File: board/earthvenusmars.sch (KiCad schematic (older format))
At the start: 30 parts, among them J1 Conn_01x05_Female, J4 Conn_01x04, SW1 SW_SPST, SW2 SW_SPST, U1 ATSAMD21G18A-AU, U2 MIC5504-3.3YM5, Y1 32768Hz

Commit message: change 1uF cap to an 0603 because the 0805 one was so thick it was impacting the case design
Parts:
- C10, C13, C7, C9: footprint Capacitor_SMD:C_0805_2012Metric -> Capacitor_SMD:C_0603_1608Metric
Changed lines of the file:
@@
 F 0 "C7" H 5408 2096 50  0000 R CNN
 F 1 "1µF" H 5408 2005 50  0000 R CNN
-F 2 "Capacitor_SMD:C_0805_2012Metric" H 5500 2050 50  0001 C CNN
+F 2 "Capacitor_SMD:C_0603_1608Metric" H 5500 2050 50  0001 C CNN
 F 3 "~" H 5500 2050 50  0001 C CNN
 	1    5500 2050
@@
 F 0 "C9" H 1058 1446 50  0000 R CNN
 F 1 "1µF" H 1058 1355 50  0000 R CNN
-F 2 "Capacitor_SMD:C_0805_2012Metric" H 1150 1400 50  0001 C CNN
+F 2 "Capacitor_SMD:C_0603_1608Metric" H 1150 1400 50  0001 C CNN
 F 3 "~" H 1150 1400 50  0001 C CNN
 	1    1150 1400
@@
 F 0 "C10" H 2308 1446 50  0000 R CNN
 F 1 "1µF" H 2308 1355 50  0000 R CNN
-F 2 "Capacitor_SMD:C_0805_2012Metric" H 2400 1400 50  0001 C CNN
+F 2 "Capacitor_SMD:C_0603_1608Metric" H 2400 1400 50  0001 C CNN
 F 3 "~" H 2400 1400 50  0001 C CNN
 	1    2400 1400
@@
 F 0 "C13" H 1150 2950 50  0000 L CNN
 F 1 "1uF" H 1100 2750 50  0000 L CNN
-F 2 "Capacitor_SMD:C_0805_2012Metric" H 1188 2700 50  0001 C CNN
+F 2 "Capacitor_SMD:C_0603_1608Metric" H 1188 2700 50  0001 C CNN
 F 3 "~" H 1150 2850 50  0001 C CNN
 	1    1150 2850

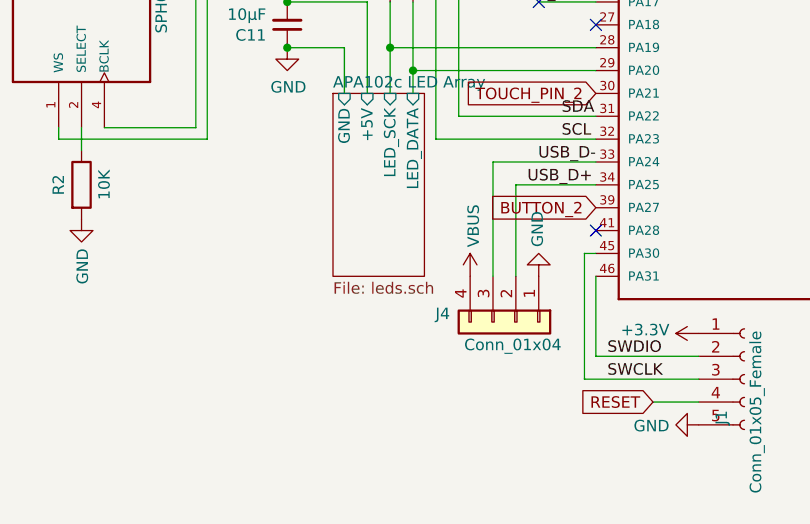
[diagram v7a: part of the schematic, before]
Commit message: add a usb-micro port (I know). including both usb styles on this prototype stage to try them both out and compare
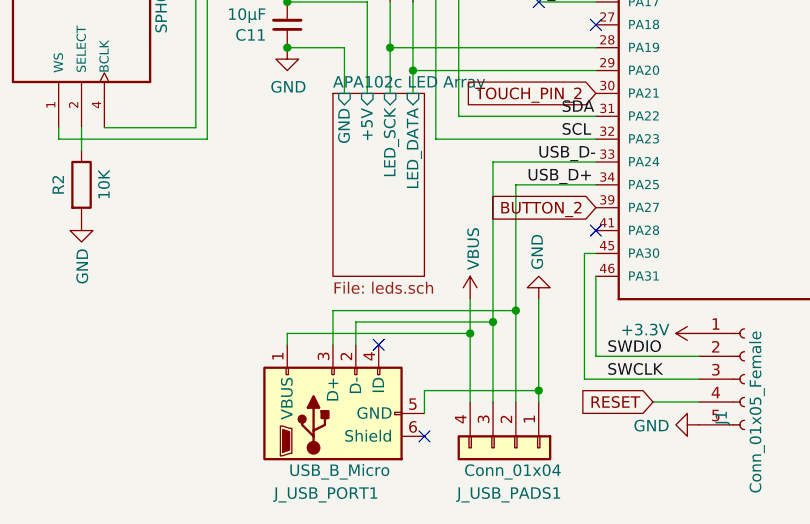
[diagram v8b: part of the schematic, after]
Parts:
- added J_USB_PORT1: USB_B_Micro, Connector_USB:USB_Micro-B_GCT_USB3076-30-A, symbol Connector:USB_B_Micro
- renumbered J4 to J_USB_PADS1
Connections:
- net GND: now also J_USB_PORT1.5 (GND)
- net USB_D+: now also J_USB_PORT1.3 (D+)
- net USB_D-: now also J_USB_PORT1.2 (D-)
- net VBUS: now also J_USB_PORT1.1 (VBUS)
- no-connect marks 19 -> 21
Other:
- moved on the sheet: J_USB_PADS1
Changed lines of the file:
@@
 L power:GND #PWR0102
 U 1 1 5EB2B290
-P 3700 4550
-F 0 "#PWR0102" H 3700 4300 50  0001 C CNN
-F 1 "GND" V 3705 4422 50  0000 R CNN
-F 2 "" H 3700 4550 50  0001 C CNN
-F 3 "" H 3700 4550 50  0001 C CNN
-	1    3700 4550
+P 3700 4650
+F 0 "#PWR0102" H 3700 4400 50  0001 C CNN
+F 1 "GND" V 3705 4522 50  0000 R CNN
+F 2 "" H 3700 4650 50  0001 C CNN
+F 3 "" H 3700 4650 50  0001 C CNN
+	1    3700 4650
 	-1   0    0    1
 $EndComp
@@
 Wire Wire Line
 	5350 1450 5350 1550
-$Comp
-L power:VBUS #PWR0103
-U 1 1 5EB2B320
-P 3400 4550
-F 0 "#PWR0103" H 3400 4400 50  0001 C CNN
-F 1 "VBUS" V 3415 4677 50  0000 L CNN
-F 2 "" H 3400 4550 50  0001 C CNN
-F 3 "" H 3400 4550 50  0001 C CNN
-	1    3400 4550
-	1    0    0    -1
-$EndComp
 Text Label 5500 1150 3    50   ~ 0
 VDDANA
@@
 	5400 1750 5500 1750
 $Comp
-L Connector_Generic:Conn_01x04 J4
+L Connector_Generic:Conn_01x04 J_USB_PADS1
 U 1 1 5F9E60C8
-P 3600 4750
-F 0 "J4" V 3564 4462 50  0000 R CNN
-F 1 "Conn_01x04" V 3700 4950 50  0000 R CNN
-F 2 "earthvenusmars:USB_SMD" H 3600 4750 50  0001 C CNN
-F 3 "~" H 3600 4750 50  0001 C CNN
-	1    3600 4750
+P 3600 5300
+F 0 "J_USB_PADS1" V 3800 5500 50  0000 R CNN
+F 1 "Conn_01x04" V 3700 5500 50  0000 R CNN
+F 2 "earthvenusmars:USB_SMD" H 3600 5300 50  0001 C CNN
+F 3 "~" H 3600 5300 50  0001 C CNN
+	1    3600 5300
 	0    1    1    0
 $EndComp
@@
 $EndComp
 Wire Wire Line
-	3500 4550 3500 4050
-Wire Wire Line
 	3500 4050 3950 4050
-Wire Wire Line
-	3600 4550 3600 4150
 Wire Wire Line
 	3600 4150 3950 4150
@@
 Wire Wire Line
 	3250 3950 3950 3950
+NoConn ~ 3000 4850
+NoConn ~ 3200 5250
+$Comp
+L Connector:USB_B_Micro J_USB_PORT1
+U 1 1 60BC4B2E
+P 2800 5150
+F 0 "J_USB_PORT1" V 2450 4950 50  0000 L CNN
+F 1 "USB_B_Micro" V 2550 4900 50  0000 L CNN
+F 2 "Connector_USB:USB_Micro-B_GCT_USB3076-30-A" H 2950 5100 50  0001 C CNN
+F 3 "~" H 2950 5100 50  0001 C CNN
+	1    2800 5150
+	0    -1   -1   0
+$EndComp
+Wire Wire Line
+	3500 4050 3500 4750
+Wire Wire Line
+	3600 4150 3600 4700
+$Comp
+L power:VBUS #PWR0103
+U 1 1 5EB2B320
+P 3400 4650
+F 0 "#PWR0103" H 3400 4500 50  0001 C CNN
+F 1 "VBUS" V 3415 4777 50  0000 L CNN
+F 2 "" H 3400 4650 50  0001 C CNN
+F 3 "" H 3400 4650 50  0001 C CNN
+	1    3400 4650
+	1    0    0    -1
+$EndComp
+Wire Wire Line
+	3200 5150 3200 5050
+Wire Wire Line
+	3500 4750 2900 4750
+Wire Wire Line
+	2900 4750 2900 4850
+Connection ~ 3500 4750
+Wire Wire Line
+	2800 4850 2800 4700
+Wire Wire Line
+	2800 4700 3600 4700
+Connection ~ 3600 4700
+Wire Wire Line
+	3700 4650 3700 5050
+Wire Wire Line
+	3600 4700 3600 5100
+Wire Wire Line
+	3500 4750 3500 5100
+Wire Wire Line
+	3400 4650 3400 4800
+Wire Wire Line
+	3200 5050 3700 5050
+Connection ~ 3700 5050
+Wire Wire Line
+	3700 5050 3700 5100
+Wire Wire Line
+	2600 4850 2600 4800
+Connection ~ 3400 4800
+Wire Wire Line
+	3400 4800 3400 5100
+Wire Wire Line
+	2600 4800 3400 4800
 $EndSCHEMATC
